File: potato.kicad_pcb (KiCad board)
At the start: 2 copper layers, 17.8 x 12.7 mm, 9 parts, among them P2 OKR-T6/10, SW1 SPST

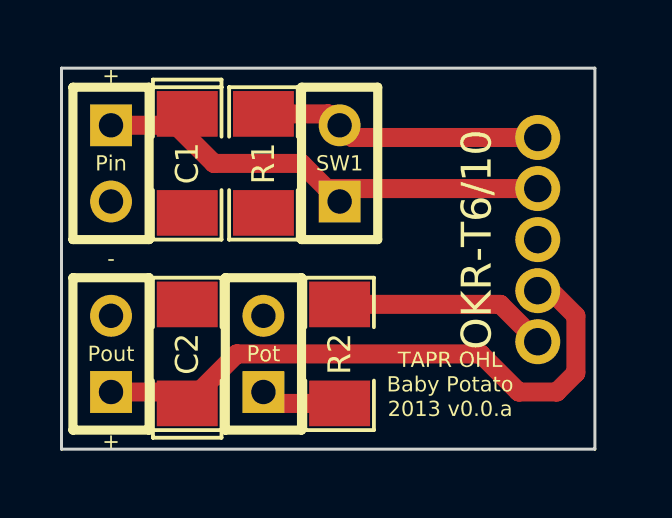
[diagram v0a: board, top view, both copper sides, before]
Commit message: Wider Traces
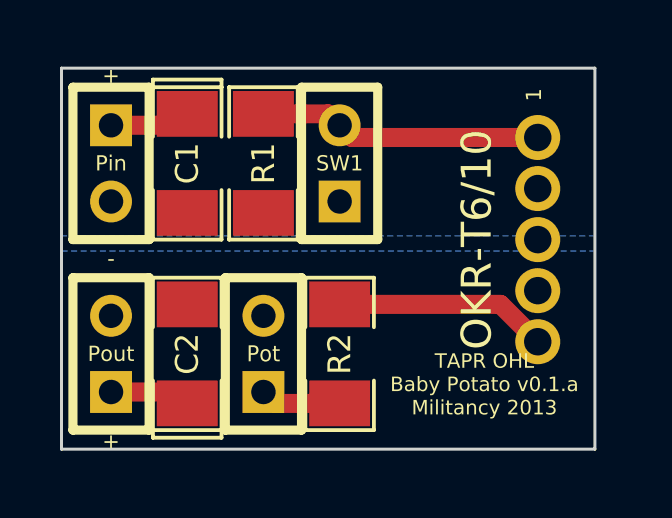
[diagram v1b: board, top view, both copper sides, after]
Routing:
- net N-000006: track 20.3 -> 2.70 mm
- net N-000005: track 15.1 -> 2.16 mm
- added copper zone on B.Cu, net N-000005
- added copper zone on B.Cu, net N-000006
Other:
- board text added: "1"
- board text added: "TAPR OHL Baby Potato v0.1.a Militancy 2013"
- board text removed: "TAPR OHL Baby Potato 2013 v0.0.a"
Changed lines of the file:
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@@
     (area 10.744288 16.160045 40.961 34.450001)
     (thickness 1.6)
-    (drawings 10)
-    (tracks 21)
+    (drawings 11)
+    (tracks 10)
     (zones 0)
     (modules 9)
@@
   (layers
     (15 F.Cu signal)
-    (0 B.Cu signal hide)
+    (0 B.Cu signal)
     (16 B.Adhes user hide)
     (17 F.Adhes user hide)
@@
     )
   )
-  (gr_text "TAPR OHL\nBaby Potato\n2013 v0.0.a" (at 33.909 28.321) (layer F.SilkS)
+  (gr_text 1 (at 36.703 18.669 90) (layer F.SilkS)
     (effects (font (size 0.508 0.508) (thickness 0.127)))
+  )
+  (gr_text "TAPR OHL\nBaby Potato v0.1.a\nMilitancy 2013" (at 35.052 28.321) (layer F.SilkS)
+    (effects (font (size 0.4826 0.4826) (thickness 0.12065)))
   )
   (dimension 17.78 (width 0.3) (layer Cmts.User)
@@
   (segment (start 30.226 28.956) (end 28.067 28.956) (width 0.635) (layer F.Cu) (net 4))
   (segment (start 28.067 28.956) (end 27.686 28.575) (width 0.635) (layer F.Cu) (net 4))
-  (segment (start 22.606 19.685) (end 24.765 19.685) (width 0.635) (layer F.Cu) (net 5))
-  (segment (start 29.7942 21.7932) (end 36.83 21.7932) (width 0.635) (layer F.Cu) (net 5) (status 20))
-  (segment (start 28.956 20.955) (end 29.7942 21.7932) (width 0.635) (layer F.Cu) (net 5))
-  (segment (start 26.035 20.955) (end 28.956 20.955) (width 0.635) (layer F.Cu) (net 5))
-  (segment (start 24.765 19.685) (end 26.035 20.955) (width 0.635) (layer F.Cu) (net 5))
-  (segment (start 36.83 25.1968) (end 37.2618 25.1968) (width 0.635) (layer F.Cu) (net 6))
-  (segment (start 25.527 28.575) (end 22.606 28.575) (width 0.635) (layer F.Cu) (net 6))
-  (segment (start 26.797 27.305) (end 25.527 28.575) (width 0.635) (layer F.Cu) (net 6))
-  (segment (start 34.925 27.305) (end 26.797 27.305) (width 0.635) (layer F.Cu) (net 6))
-  (segment (start 36.195 28.575) (end 34.925 27.305) (width 0.635) (layer F.Cu) (net 6))
-  (segment (start 37.465 28.575) (end 36.195 28.575) (width 0.635) (layer F.Cu) (net 6))
-  (segment (start 38.1 27.94) (end 37.465 28.575) (width 0.635) (layer F.Cu) (net 6))
-  (segment (start 38.1 26.035) (end 38.1 27.94) (width 0.635) (layer F.Cu) (net 6))
-  (segment (start 37.2618 25.1968) (end 38.1 26.035) (width 0.635) (layer F.Cu) (net 6))
+  (segment (start 22.606 19.685) (end 24.765 19.685) (width 0.635) (layer F.Cu) (net 5) (status 10))
+  (segment (start 22.606 28.575) (end 24.765 28.575) (width 0.635) (layer F.Cu) (net 6) (status 10))
+  (segment (start 24.765 28.575) (end 25.146 28.956) (width 0.635) (layer F.Cu) (net 6))
   (zone (net 1) (net_name GND) (layer F.Cu) (hatch edge 0.508)
     (connect_pads (clearance 0.254))
@@
       )
     )
+  )
+  (zone (net 5) (net_name N-000005) (layer B.Cu) (hatch edge 0.508)
+    (connect_pads (clearance 0.254))
+    (min_thickness 0.254)
+    (fill (arc_segments 16) (thermal_gap 0.381) (thermal_bridge_width 1.016))
+    (polygon
+      (pts
+        (xy 38.735 23.368) (xy 20.955 23.368) (xy 20.955 17.78) (xy 38.735 17.78)
+      )
+    )
+  )
+  (zone (net 6) (net_name N-000006) (layer B.Cu) (hatch edge 0.508)
+    (connect_pads (clearance 0.254))
+    (min_thickness 0.254)
+    (fill (arc_segments 16) (thermal_gap 0.381) (thermal_bridge_width 1.016))
+    (polygon
+      (pts
+        (xy 38.735 30.48) (xy 20.955 30.48) (xy 20.955 23.876) (xy 38.735 23.876)
+      )
+    )
